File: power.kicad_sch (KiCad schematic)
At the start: 23 parts, among them J2 532610271, Q1 NTK3139P, U2 BQ25170J, U3 TPS62840DLCR

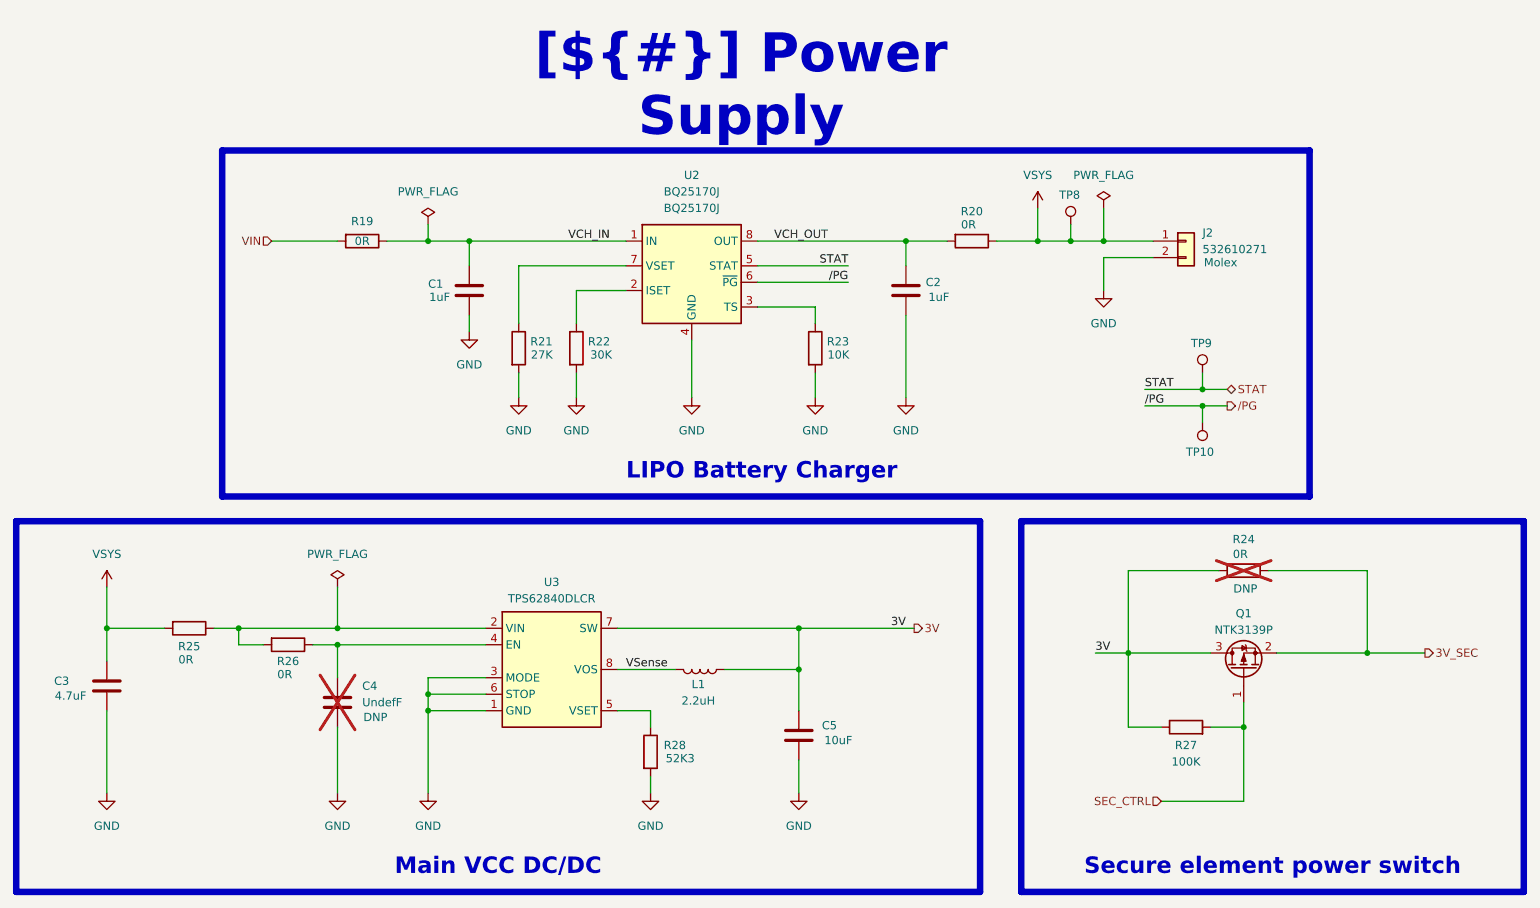
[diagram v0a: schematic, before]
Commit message: fix(hardware): replace jumper/passive footprints with 0402 and refine schematics
- Replace 0-ohm jumper resistors with 0402 package equivalents
- Reduce package size on several capacitors
- Correct and simplify several schematic symbols (replaced with
  simplified equivalents where the original was overcomplicated)
- Bump lib submodule to the updated component library (renamed
  switch footprints, new Conn_01x02_MountingPin symbol, pad/pin
  numbering fixes, approved IPN assignments, Workart artwork library)
- Register Workart.pretty in fp-lib-table
- Mark J3 as DNP in mcu.kicad_sch
- Continue schematic wiring/placement (Leds.kicad_sch, tessera.kicad_sch)
  and PCB routing/placement (tessera.kicad_pcb)
- Add board outline source (Images/pcb_size.dxf, pcb_shape.FCStd) and
  silkscreen artwork sources (Logos/) for the Workart footprints
- Complete preliminary version of PCB
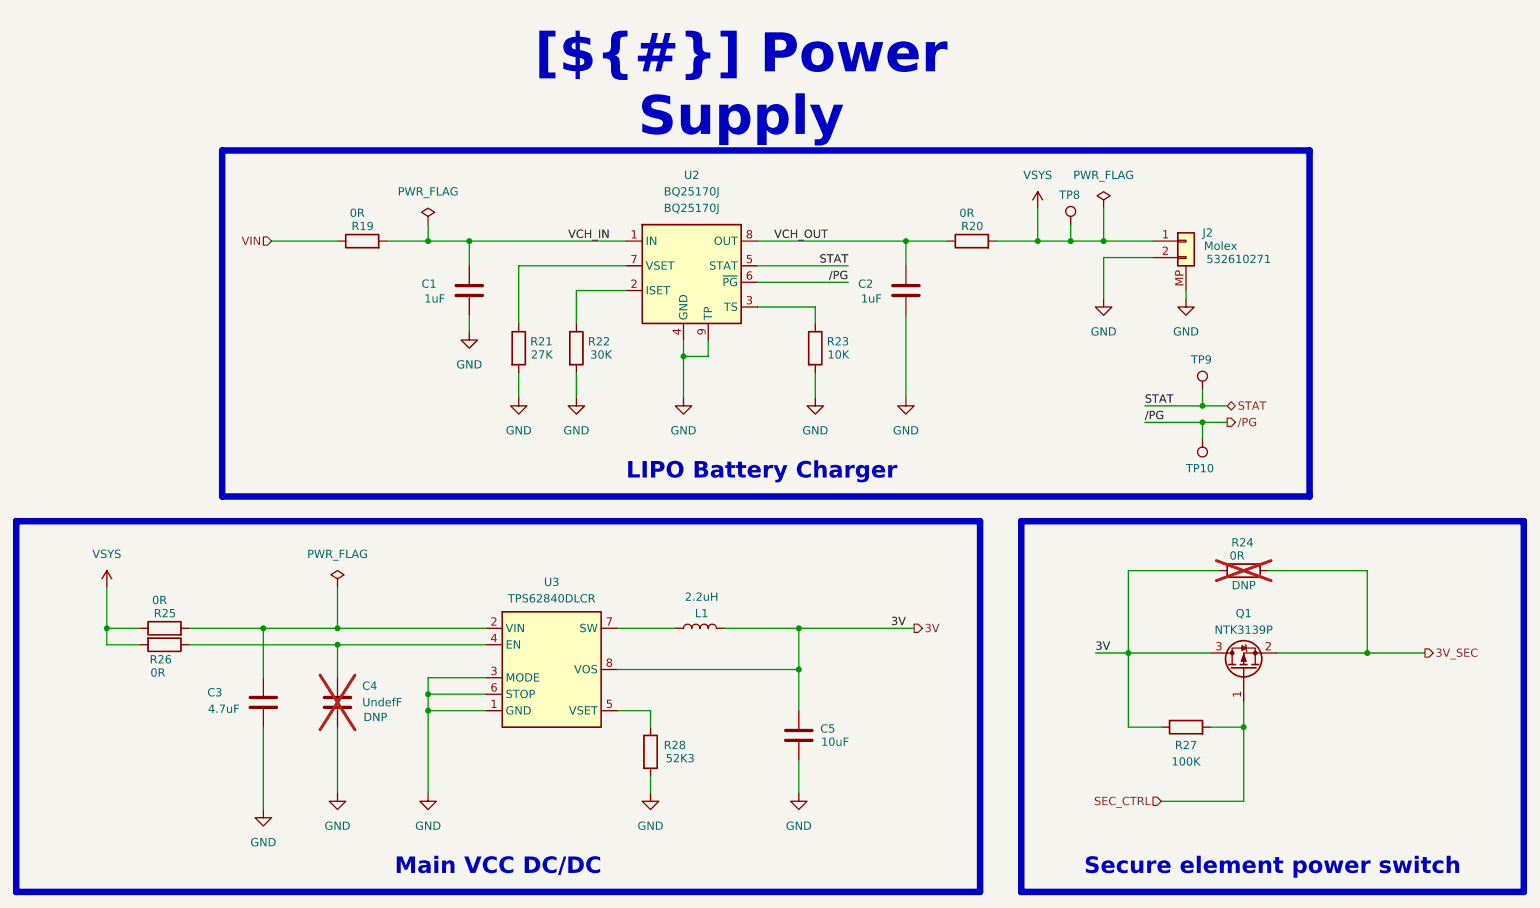
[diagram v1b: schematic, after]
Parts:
- removed C1, C2: 1uF 50V (X7R), Capacitor_SMD:C_0805_2012Metric, symbol catalog:Capacitors/C0805_1uF_50V_±10%_X7R
- removed C3: 4.7uF 50V (X7R), Capacitor_SMD:C_1206_3216Metric, symbol catalog:Capacitors/C1206_4.7uF_50V_±10%_X7R
- removed C5: 10uF 50V (X7R), Capacitor_SMD:C_1210_3225Metric, symbol catalog:Capacitors/C1210_10uF_50V_±10%_X7R
- removed R19, R20, R24, R25, R26: 0R ±5% 1/10W, Resistor_SMD:R_0603_1608Metric, symbol catalog:Resistors/R0603_0R_0.1W_±5%
- added C1, C2: 1uF 6.3V (X5R), Capacitor_SMD:C_0402_1005Metric, symbol catalog:Capacitors/C0402_1uF_6.3V_±10%_X5R
- added C3: 4.7uF 6.3V (X7R), Capacitor_SMD:C_0805_2012Metric, symbol catalog:Capacitors/C0805_4.7uF_6.3V_±10%_X7R
- added C5: 10uF 10V (X7R), Capacitor_SMD:C_0805_2012Metric, symbol catalog:Capacitors/C0805_10uF_10V_±10%_X7R
- added R19, R20, R24, R25, R26: 0R ±5% 1/16W, Resistor_SMD:R_0402_1005Metric, symbol catalog:Resistors/R0402_0R_0.1W_±5%
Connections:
- net VSense is gone; now on net 3V: L1.2, U3.8 (VOS)
- net 3V: now also C5.1, R24.1; no longer L1.1, U3.7 (SW)
- net 3V_SEC: now also R24.2
- net GND: now also J2.MP, U2.9 (TP), C1.2, C2.2, C3.2, C5.2
- net VCH_IN: now also C1.1, R19.2
- net VCH_OUT: now also C2.1, R20.1
- net VIN: now also R19.1
- net VSYS: now also R20.2, R25.1, R26.2
- net at C4.1, U3.4 (EN): now also R26.1
- net at U3.2 (VIN): now also C3.1, R25.2
- new net: L1.1, U3.7 (SW)
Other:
- moved on the sheet: L1, TP10, TP9

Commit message: fix(hardware): tighten PCB edge clearance and diff-pair rules, update logo
- Bump lib submodule: assign IPNs to another batch of approved
  capacitor selections
- Update the embedded logo artwork on every schematic sheet to the
  new Logos/logo.png
- Increase min_copper_edge_clearance to 0.5mm and raise net class
  clearance/spacing to match
- Replace the generic outer/inner-layer trace width & spacing rules
  with a dedicated "USB Diff Pair clearance to other nets" rule
  (0.2023mm, excluding intra-pair spacing already governed by the
  netclass diff_pair_gap)
- Add DRC exclusions for pre-existing clearance/copper-edge/solder-
  mask-bridge items surfaced by the tightened edge-clearance rule
- Continue schematic placement and PCB routing/placement
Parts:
- C1, C2: IPN IPN_C-???? -> IPN_C-0008

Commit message: feat(hardware): route debug UART to J3 and add charger status pull-ups
Exposes a spare UART on the SWD header for firmware logging and adds
external pull-ups to the BQ25170 open-drain status outputs.

- Route P0.22 (UART_TX) to J3 pin 7 and P0.20 (UART_RX) to J3 pin 8.
- Add R44/R45 100k pull-ups to VCC on CHG_STAT and CHG_PG.
- Update PCB placement and routing for the new nets.
- Bump lib submodule (new THT test point footprint).
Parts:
- added R44, R45: 100 kOhms, Resistor_SMD:R_0402_1005Metric, symbol catalog:Resistors/R0402_100K_0.063W_±1%
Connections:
- net 3V: now also R44.2, R45.2
- net STAT: now also R44.1
- net /PG: now also R45.1
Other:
- moved on the sheet: C1, C2, J2, R19, R20, R21, R22, R23, TP10, TP8, TP9, U2
